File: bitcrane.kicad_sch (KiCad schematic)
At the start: 75 parts, among them J1 PSU Comm, J12 0455580003, J13 Hashboard0, J3 61900411021, J4 61900411021, J6 USB_C_Receptacle_USB2.0, J7 0353180420, J8 0353180420, Q1 DMP3013SFV-7, U1 FT4232HQ-REEL, U2 RT9080-33GJ5, U3 M93C46-WDW6TP, U5 EMC2305-1-AP-TR, Y1 12MHz

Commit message: added fixes for #2 #3 #4 to schematic. still needs to be adjusted in layout
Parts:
- removed TP6 (x4): TestPoint, TestPoint:TestPoint_Pad_D1.5mm, symbol Connector:TestPoint
- added R17: 33k, Resistor_SMD:R_0402_1005Metric, symbol Device:R_US
- added R18: 22k, Resistor_SMD:R_0402_1005Metric, symbol Device:R_US
- added R19: 4.7k, Resistor_SMD:R_0402_1005Metric, symbol Device:R_US
- added TP6 (x2): TestPoint, TestPoint:TestPoint_Pad_D1.5mm, symbol Connector:TestPoint
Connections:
- net FAN_ALERT: now also U1.30 (BDBUS4), R19.1; no longer U1.55 (DDBUS4)
- net PLUG: now also U1.19 (ADBUS3); no longer U1.30 (BDBUS4)
- net PSU_EN: now also U1.32 (BDBUS5); no longer U1.43 (CDBUS4)
- net RST: now also U1.21 (ADBUS4); no longer U1.32 (BDBUS5)
- net RXD: now also U1.39 (CDBUS1); no longer U1.17 (ADBUS1)
- net SCL: now also J1.6 (Pin_6), U5.2 (SMCLK); no longer J13.4 (Pin_4)
- net SDA: now also J1.3 (Pin_3), U1.28 (BDBUS2), U5.1 (SMDATA); no longer J13.3 (Pin_3)
- net TXD: now also U1.38 (CDBUS0); no longer U1.16 (ADBUS0)
- net VCCIO: now also R17.2, R18.2, R19.2
- net HB_SDA: now reaches U1.18 (ADBUS2)
- net HB_SDA: now also J13.3 (Pin_3), U1.17 (ADBUS1), TP6.1
- net at U5.11 (CLK): now also R18.1
- net at U5.4 (ADDR_SEL): now also R17.1
- net FAN_SCL: no longer names the net of U1.48 (DDBUS0)
- net FAN_SCL: no longer U5.2 (SMCLK)
- net FAN_SDA: no longer names the net of U1.52 (DDBUS1)
- net FAN_SDA: no longer U5.1 (SMDATA)
- removed net PSU_SCL: J1.6 (Pin_6), U1.38 (CDBUS0)
- removed net PSU_SDA: J1.3 (Pin_3), U1.39 (CDBUS1)
- new net HB_SCL: J13.4 (Pin_4), TP6.1, U1.16 (ADBUS0)
- no-connect marks 30 -> 28
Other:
- moved on the sheet: J1, TP6

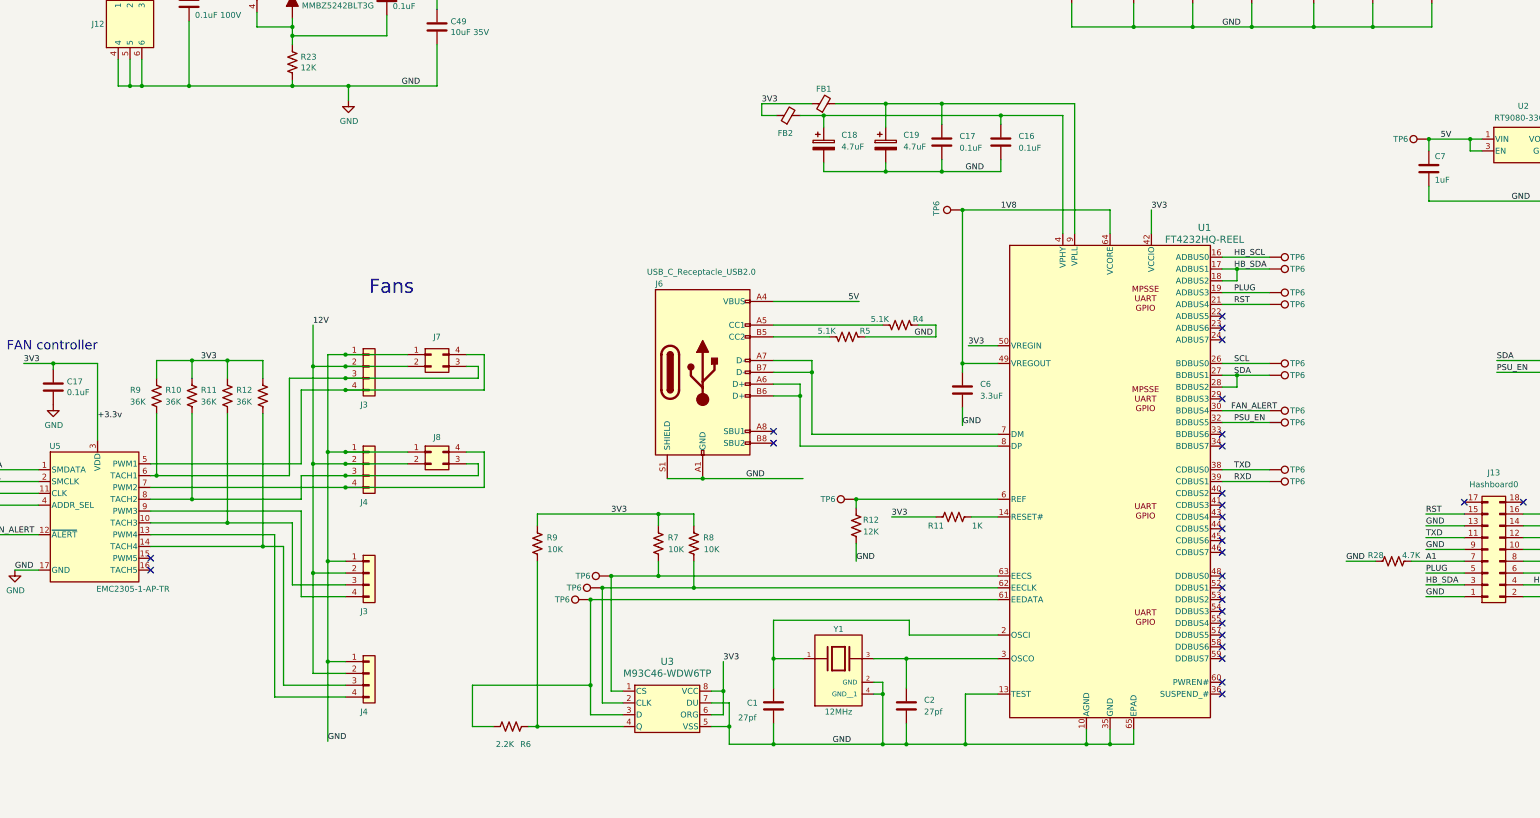
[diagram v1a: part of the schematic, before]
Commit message: added fix for #5 to schematic. still needs PCB work
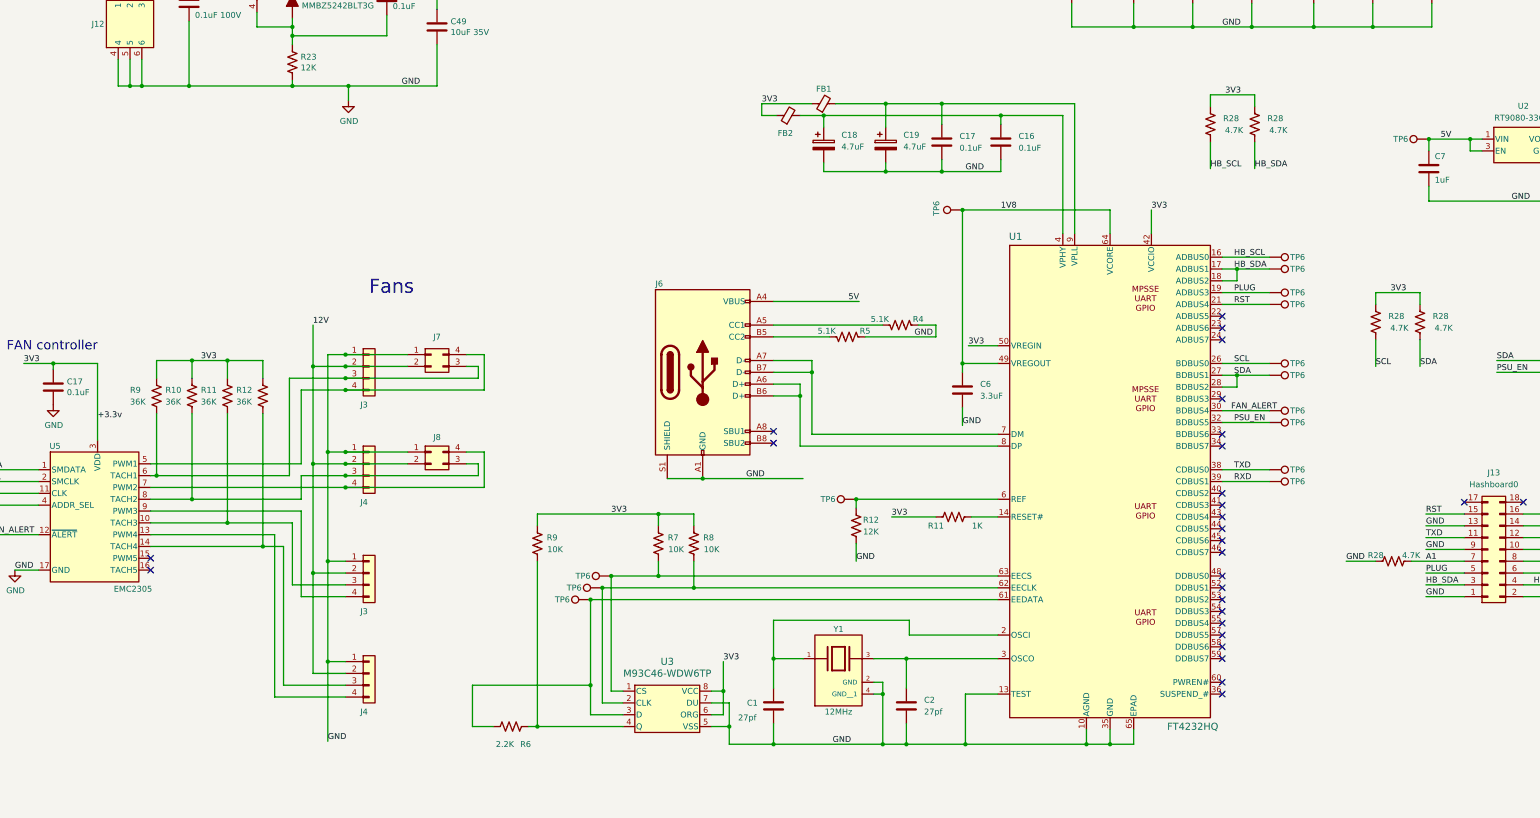
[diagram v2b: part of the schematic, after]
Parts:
- added R28 (x4): 4.7K, Resistor_SMD:R_0402_1005Metric, symbol Device:R_US
- U1: value FT4232HQ-REEL -> FT4232HQ
- U5: value EMC2305-1-AP-TR -> EMC2305
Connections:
- net HB_SCL: now also R28.1
- net HB_SDA: now also R28.1
- net SCL: now also R28.1
- net SDA: now also R28.1
- net VCCIO: now also R28.2, R28.2, R28.2, R28.2

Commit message: routed v2 changes
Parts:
- added H1, H2, H3, H4: MountingHole_Pad, bitcrane:MountingHole_3mm_Pad, symbol Mechanical:MountingHole_Pad
- added J16, J17: 0353180420, bitcrane:MOLEX_353180420, symbol Connector_Generic:Conn_02x02_Counter_Clockwise
- C1, C2: footprint Capacitor_SMD:C_0402_1005Metric -> Capacitor_SMD:C_0805_2012Metric; DK 1292-1291-1-ND -> (none); PARTNO 0402N270J250CT -> (none)
- C10, C11, C12, C13, C14, C15, C16, C17, C48, C9: footprint Capacitor_SMD:C_0402_1005Metric -> Capacitor_SMD:C_0805_2012Metric; DK 478-KGM05AR71C104KHCT-ND -> (none); PARTNO KGM05AR71C104KH -> (none)
- C43: footprint Capacitor_SMD:C_0402_1005Metric -> Capacitor_SMD:C_0805_2012Metric; DK 490-10458-1-ND -> (none); PARTNO GRM155R62A104KE14D -> (none)
- C7, C8: footprint Capacitor_SMD:C_0402_1005Metric -> Capacitor_SMD:C_0805_2012Metric; DK 587-5514-1-ND -> (none); PARTNO EMK105BJ105MV-F -> (none)
- R10, R11, R12, R9: footprint Resistor_SMD:R_0402_1005Metric -> Resistor_SMD:R_0805_2012Metric; DK CR0402-FX-3602GLFCT-ND -> (none); PARTNO CR0402-FX-3602GLF -> (none)
- R11: footprint Resistor_SMD:R_0402_1005Metric -> Resistor_SMD:R_0805_2012Metric; DK 311-1.00KLRCT-ND -> (none); PARTNO RC0402FR-071KL -> (none)
- R12, R23: footprint Resistor_SMD:R_0402_1005Metric -> Resistor_SMD:R_0805_2012Metric; DK RC0402FR-1312KL -> (none); PARTNO RC0402FR-1312KL -> (none)
- R17, R18: footprint Resistor_SMD:R_0402_1005Metric -> Resistor_SMD:R_0805_2012Metric
- R19, R28, R31, R33: footprint Resistor_SMD:R_0402_1005Metric -> Resistor_SMD:R_0805_2012Metric; DK 311-4.7KLRCT-ND -> (none); PARTNO RC0402FR-074K7L -> (none)
- R4, R5: footprint Resistor_SMD:R_0402_1005Metric -> Resistor_SMD:R_0805_2012Metric; DK RMCF0402JT5K10CT-ND -> (none); PARTNO RMCF0402JT5K10 -> (none)
- R6: footprint Resistor_SMD:R_0402_1005Metric -> Resistor_SMD:R_0805_2012Metric; DK 311-2.20KLRCT-ND -> (none); PARTNO RC0402FR-072K2L -> (none)
- R7, R8, R9: footprint Resistor_SMD:R_0402_1005Metric -> Resistor_SMD:R_0805_2012Metric; DK RMCF0402FT10K0CT-ND -> (none); PARTNO RMCF0402FT10K0 -> (none)
- renumbered J7 to J14, J8 to J15, J6 to J8
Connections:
- net 12V: now also J16.2 (Pin_2), J17.2 (Pin_2)
- net GND: now also H1.1, H2.1, H3.1, H4.1, J16.1 (Pin_1), J17.1 (Pin_1)
- net at J4.3 (Pin_3), R12.2, U5.14 (TACH4): now also J17.3 (Pin_3)
- net at J4.4 (Pin_4), U5.13 (PWM4): now also J17.4 (Pin_4)
- net at J3.3 (Pin_3), R11.2, U5.10 (TACH3): now also J16.3 (Pin_3)
- net at J3.4 (Pin_4), U5.9 (PWM3): now also J16.4 (Pin_4)
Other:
- moved on the sheet: J4

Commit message: switched to 3 HB connectors. added I2C hub. routed
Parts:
- removed R28 (x2): 4.7K, Resistor_SMD:R_0805_2012Metric, symbol Device:R_US
- removed TP6 (x2): TestPoint, TestPoint:TestPoint_Pad_D1.5mm, symbol Connector:TestPoint
- added C17: 0.1uF, Capacitor_SMD:C_0805_2012Metric, symbol Device:C
- added J13: Hashboard1, bitcart:CONN-TH_X2026WV-2-09D-46SN, symbol Connector_Generic:Conn_02x09_Odd_Even
- added J13: Hashboard2, bitcart:CONN-TH_X2026WV-2-09D-46SN, symbol Connector_Generic:Conn_02x09_Odd_Even
- added R28 (x19), R31 (x2), R33 (x2): 4.7K, Resistor_SMD:R_0805_2012Metric, symbol Device:R_US
- added TP6 (x9): TestPoint, TestPoint:TestPoint_Pad_D1.5mm, symbol Connector:TestPoint
- added U10: PCA9546ARGVR, bitcart:QFN-16_EP_4x4_Pitch0.65mm, symbol bitcart:PCA9546ARGVR
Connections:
- net FAN_ALERT: now also U1.19 (ADBUS3); no longer U1.30 (BDBUS4)
- net GND: now also C17.2, J13.1 (Pin_1), J13.1 (Pin_1), J13.10 (Pin_10), J13.10 (Pin_10), J13.13 (Pin_13), J13.13 (Pin_13), J13.14 (Pin_14), J13.14 (Pin_14), J13.2 (Pin_2), J13.2 (Pin_2), J13.9 (Pin_9), J13.9 (Pin_9), R28.1, R28.1, R31.2, R31.2, R33.2, R33.2, U10.11 (A2), U10.15 (A0), U10.16 (A1), U10.17 (EPAD), U10.6 (GND)
- net PSU_EN: now also U1.21 (ADBUS4); no longer U1.32 (BDBUS5)
- net SCL: now also TP6.1, U1.16 (ADBUS0), U10.12 (SCL); no longer J1.6 (Pin_6), U1.26 (BDBUS0), U5.2 (SMCLK)
- net SDA: now also TP6.1, U1.17 (ADBUS1), U1.18 (ADBUS2), U10.13 (SDA); no longer J1.3 (Pin_3), U1.27 (BDBUS1), U1.28 (BDBUS2), U5.1 (SMDATA)
- net VCCIO: now also C17.1, J13.16 (Pin_16), J13.16 (Pin_16), R28.1, R28.1, R28.1, R28.1, R28.1, R28.1, R28.1, R28.1, R28.1, R28.2, R28.2, R28.2, R28.2, R28.2, R28.2, R28.2, R28.2, U10.14 (VCC)
- net RESET: now reaches U1.22 (ADBUS5)
- net RESET: now also TP6.1, U10.1 (*RESET)
- net RST0: now reaches U1.29 (BDBUS3)
- net RST0: now also J13.15 (Pin_15), TP6.1
- net PLUG1: now reaches U1.40 (CDBUS2)
- net PLUG1: now also J13.5 (Pin_5), TP6.1
- net RST1: now reaches U1.41 (CDBUS3)
- net RST1: now also J13.15 (Pin_15), TP6.1
- net TXD2: now reaches U1.48 (DDBUS0)
- net TXD2: now also J13.11 (Pin_11), TP6.1
- net RXD2: now reaches U1.52 (DDBUS1)
- net RXD2: now also J13.12 (Pin_12), TP6.1
- net PLUG2: now reaches U1.53 (DDBUS2)
- net PLUG2: now also J13.5 (Pin_5), TP6.1
- net RST2: now reaches U1.54 (DDBUS3)
- net RST2: now also J13.15 (Pin_15), TP6.1
- net A0 renamed A00
- net A00: now also R28.2
- net A1 renamed A10
- net A10: now also R28.2
- net A2 renamed A20
- net A20: now also R28.2
- removed net HB_SCL: J13.4 (Pin_4), TP6.1, U1.16 (ADBUS0)
- removed net HB_SDA: J13.3 (Pin_3), TP6.1, U1.17 (ADBUS1), U1.18 (ADBUS2)
- net PLUG renamed PLUG0
- net PLUG0: now also U1.28 (BDBUS2); no longer U1.19 (ADBUS3)
- removed net RST: J13.15 (Pin_15), TP6.1, U1.21 (ADBUS4)
- net RXD renamed RXD1
- net RXD1: now also J13.12 (Pin_12); no longer J13.12 (Pin_12)
- net TXD renamed TXD1
- net TXD1: now also J13.11 (Pin_11); no longer J13.11 (Pin_11)
- new net A01: J13.8 (Pin_8), R28.2, R31.1
- new net A02: J13.8 (Pin_8), R28.2, R31.1
- new net A11: J13.7 (Pin_7), R28.2, R28.2
- new net A12: J13.7 (Pin_7), R28.2, R28.2
- new net A21: J13.6 (Pin_6), R28.2, R33.1
- new net A22: J13.6 (Pin_6), R28.2, R33.1
- new net RXD0: J13.12 (Pin_12), TP6.1, U1.27 (BDBUS1)
- new net SCL0: J13.4 (Pin_4), R28.1, U10.3 (SC0)
- new net SCL1: J13.4 (Pin_4), R28.1, U10.5 (SC1)
- new net SCL2: J13.4 (Pin_4), R28.1, U10.8 (SC2)
- new net SCL3: J1.6 (Pin_6), R28.1, U10.10 (SC3), U5.1 (SMDATA)
- new net SDA0: J13.3 (Pin_3), R28.1, U10.2 (SD0)
- new net SDA1: J13.3 (Pin_3), R28.1, U10.4 (SD1)
- new net SDA2: J13.3 (Pin_3), R28.1, U10.7 (SD2)
- new net SDA3: J1.3 (Pin_3), R28.1, U10.9 (SD3), U5.2 (SMCLK)
- new net TXD0: J13.11 (Pin_11), TP6.1, U1.26 (BDBUS0)
- no-connect marks 28 -> 24
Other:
- moved on the sheet: R28, R31, R33, TP6

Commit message: ran DRC, fixed errors, generated gerbers, generated BOM
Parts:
- C1, C2: DK (none) -> 1276-2622-1-ND; PARTNO (none) -> CL21C270JCANNNC
- C10, C11, C12, C13, C14, C15, C16, C17, C43, C48, C9: DK (none) -> 1276-6840-1-ND; PARTNO (none) -> CL21B104KCFNNNE
- C7, C8: DK (none) -> 1276-1066-1-ND; PARTNO (none) -> CL21B105KAFNNNE
- H1, H2, H3, H4: now left out of the parts list
- J13: DK 455-B18B-PHDSS-ND -> (none)
- R10, R11, R12, R9: DK (none) -> 311-36.0KCRCT-ND; PARTNO (none) -> RC0805FR-0736KL
- R11: DK (none) -> RMCF0805FT1K00CT-ND; PARTNO (none) -> RMCF0805FT1K00
- R12, R23: DK (none) -> RMCF0805FT12K0CT-ND; PARTNO (none) -> RMCF0805FT12K0
- R17: DK (none) -> 311-33.0KCRCT-ND; PARTNO (none) -> RC0805FR-0733KL
- R18: DK (none) -> RMCF0805FT22K0CT-ND; PARTNO (none) -> RMCF0805FT22K0
- R19, R28, R31, R33: DK (none) -> 311-4.70KCRCT-ND; PARTNO (none) -> RC0805FR-074K7L
- R4, R5: DK (none) -> 311-5.10KCRCT-ND; PARTNO (none) -> RC0805FR-075K1L
- R6: DK (none) -> RMCF0805FT2K20CT-ND; PARTNO (none) -> RMCF0805FT2K20
- R7, R8, R9: DK (none) -> RMCF0805FT10K0CT-ND; PARTNO (none) -> RMCF0805FT10K0

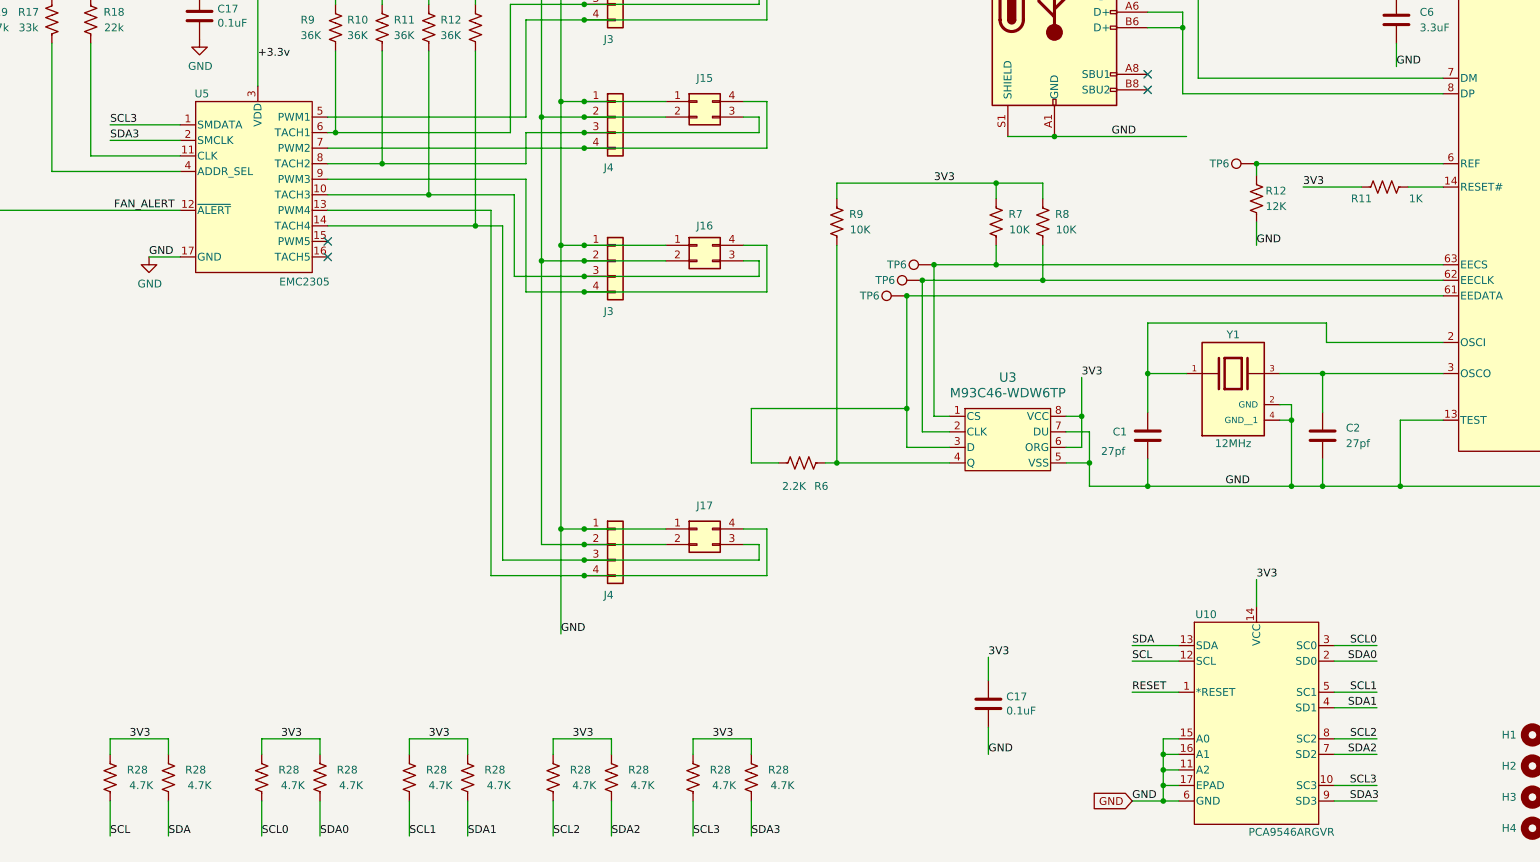
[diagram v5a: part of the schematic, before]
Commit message: fix for #8. regenerated gerbers. bump version to 2.1
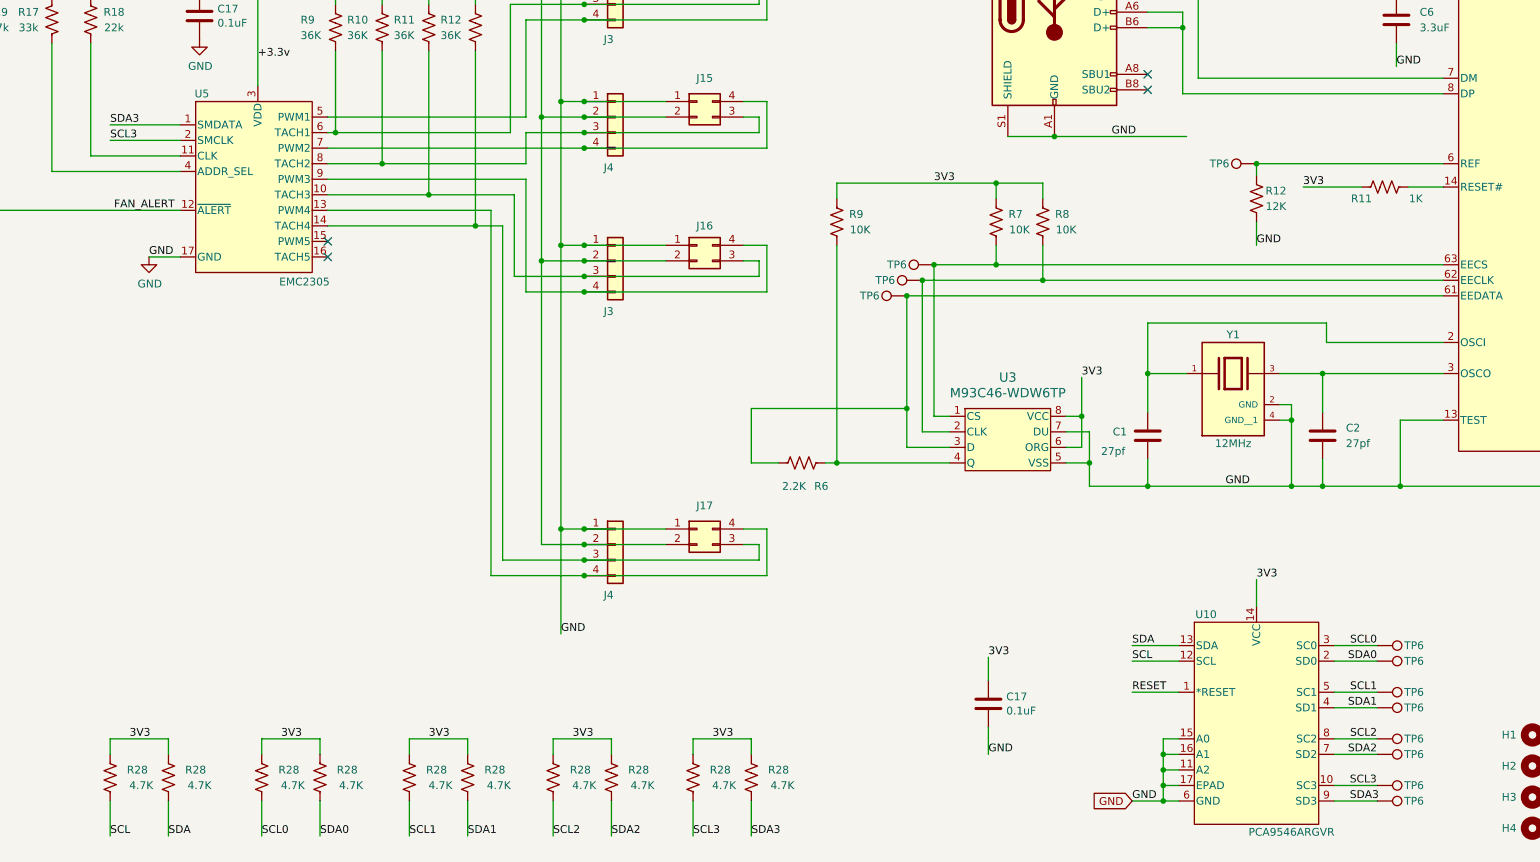
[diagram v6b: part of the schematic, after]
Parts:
- added TP6 (x8): TestPoint, TestPoint:TestPoint_Pad_D1.5mm, symbol Connector:TestPoint
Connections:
- net SCL0: now also TP6.1
- net SCL1: now also TP6.1
- net SCL2: now also TP6.1
- net SCL3: now also U5.2 (SMCLK), TP6.1; no longer U5.1 (SMDATA)
- net SDA0: now also TP6.1
- net SDA1: now also TP6.1
- net SDA2: now also TP6.1
- net SDA3: now also U5.1 (SMDATA), TP6.1; no longer U5.2 (SMCLK)

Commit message: fix for #9. regenerated gerbers. bumped version to 2.2
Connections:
- net FAN_ALERT: now also U1.23 (ADBUS6); no longer U1.19 (ADBUS3)
- net PLUG0: now also TP6.1, U1.29 (BDBUS3); no longer TP6.1, U1.28 (BDBUS2)
- net PLUG1: now also TP6.1, U1.41 (CDBUS3); no longer TP6.1, U1.40 (CDBUS2)
- net PLUG2: now also TP6.1, U1.54 (DDBUS3); no longer TP6.1, U1.53 (DDBUS2)
- net RST0: now also TP6.1, U1.28 (BDBUS2); no longer TP6.1, U1.29 (BDBUS3)
- net RST1: now also TP6.1, U1.40 (CDBUS2); no longer TP6.1, U1.41 (CDBUS3)
- net RST2: now also TP6.1, U1.53 (DDBUS2); no longer TP6.1, U1.54 (DDBUS3)
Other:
- moved on the sheet: C1, C10, C11, C12, C16, C17, C19, C43, C49, C6, C7, C8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

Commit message: fix for #10 small DRC fixes. updated to v2.3
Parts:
- added R22, R23, R47, R48: 10K, Resistor_SMD:R_0805_2012Metric, symbol Device:R_US
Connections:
- net 5V: now also R22.2, R23.2, R47.2, R48.2
- net TACH1: now reaches J14.3 (Pin_3), J3.3 (Pin_3), R9.2, U5.6 (TACH1)
- net PWM1: now reaches J14.4 (Pin_4), J3.4 (Pin_4), U5.5 (PWM1)
- net PWM1: now also R22.1
- net at TP6.1, U1.61 (EEDATA), U3.3 (D): now also R6.2; no longer R6.1
- net at R9.1, U3.4 (Q): now also R6.1; no longer R6.2
- net TACH4: now reaches J17.3 (Pin_3), J4.3 (Pin_3), R12.2, U5.14 (TACH4)
- net PWM4: now reaches J17.4 (Pin_4), J4.4 (Pin_4), U5.13 (PWM4)
- net PWM4: now also R48.1
- net TACH2: now reaches J15.3 (Pin_3), J4.3 (Pin_3), R10.2, U5.8 (TACH2)
- net PWM2: now reaches J15.4 (Pin_4), J4.4 (Pin_4), U5.7 (PWM2)
- net PWM2: now also R23.1
- net TACH3: now reaches J16.3 (Pin_3), J3.3 (Pin_3), R11.2, U5.10 (TACH3)
- net PWM3: now reaches J16.4 (Pin_4), J3.4 (Pin_4), U5.9 (PWM3)
- net PWM3: now also R47.1
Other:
- note added: "I2C Address: 0x4D"
- note added: "I2C Address: 0x70"
- moved on the sheet: C1, C10, C11, C12, C13, C14, C15, C16, C17, C18, C19, C2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
